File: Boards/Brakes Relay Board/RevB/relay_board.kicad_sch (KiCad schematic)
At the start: 9 parts, among them J1 Screw_Terminal_01x04, J2 Screw_Terminal_01x04, J3 Screw_Terminal_01x04, J4 Screw_Terminal_01x04, J5 Conn_02x10_Counter_Clockwise, J6 Conn_02x12_Counter_Clockwise, J7 Screw_Terminal_01x04

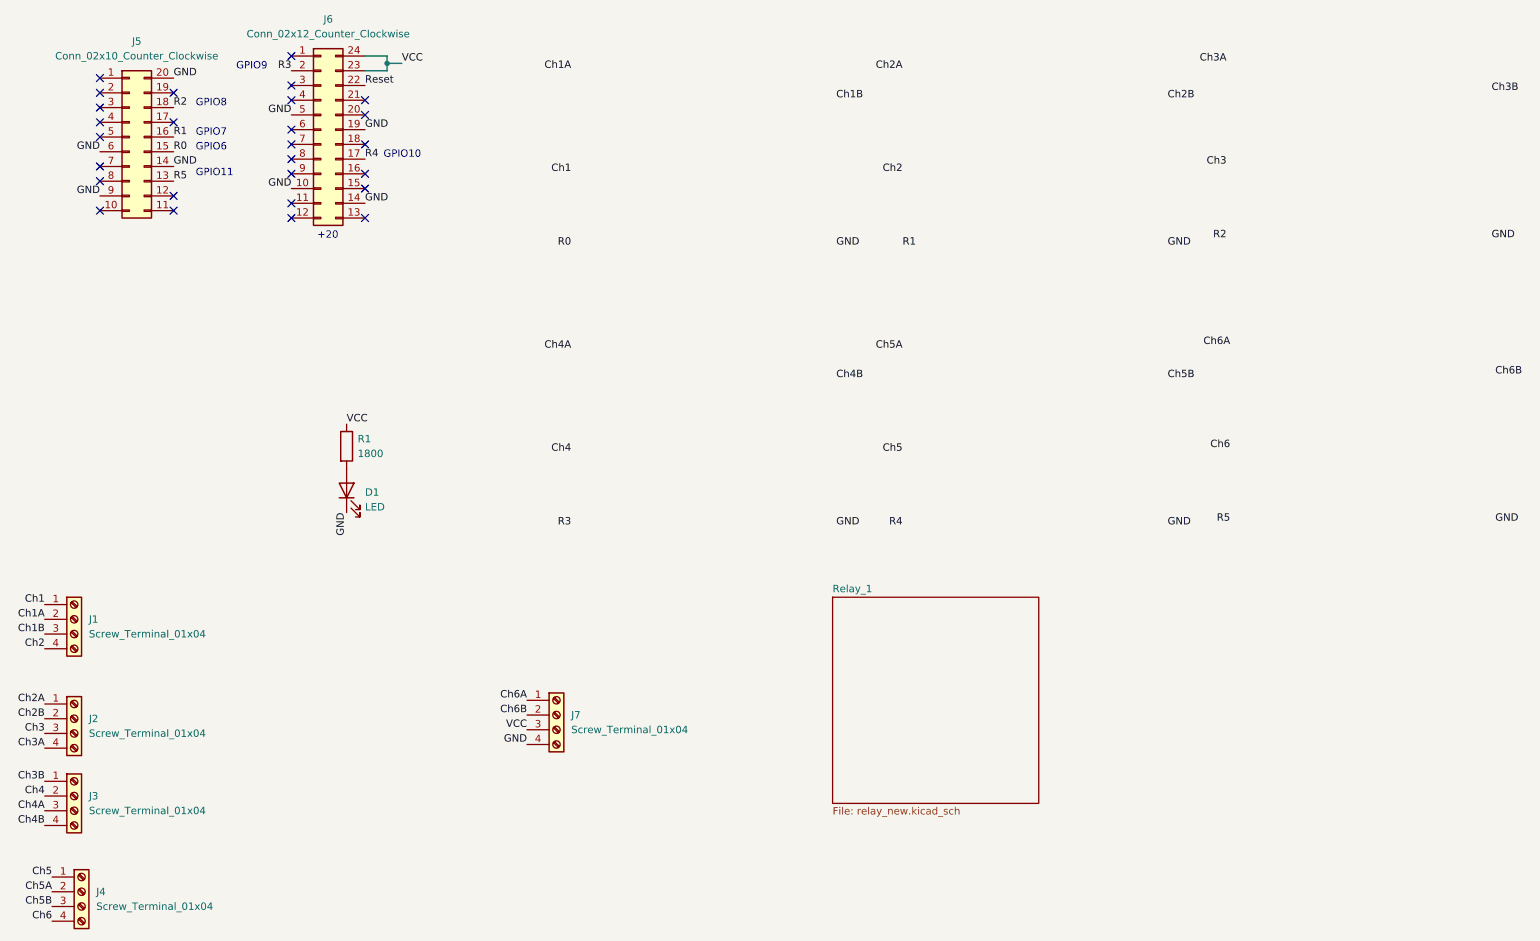
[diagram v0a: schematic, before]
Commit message: Added mosfet to relay and 5V regulator to schematic
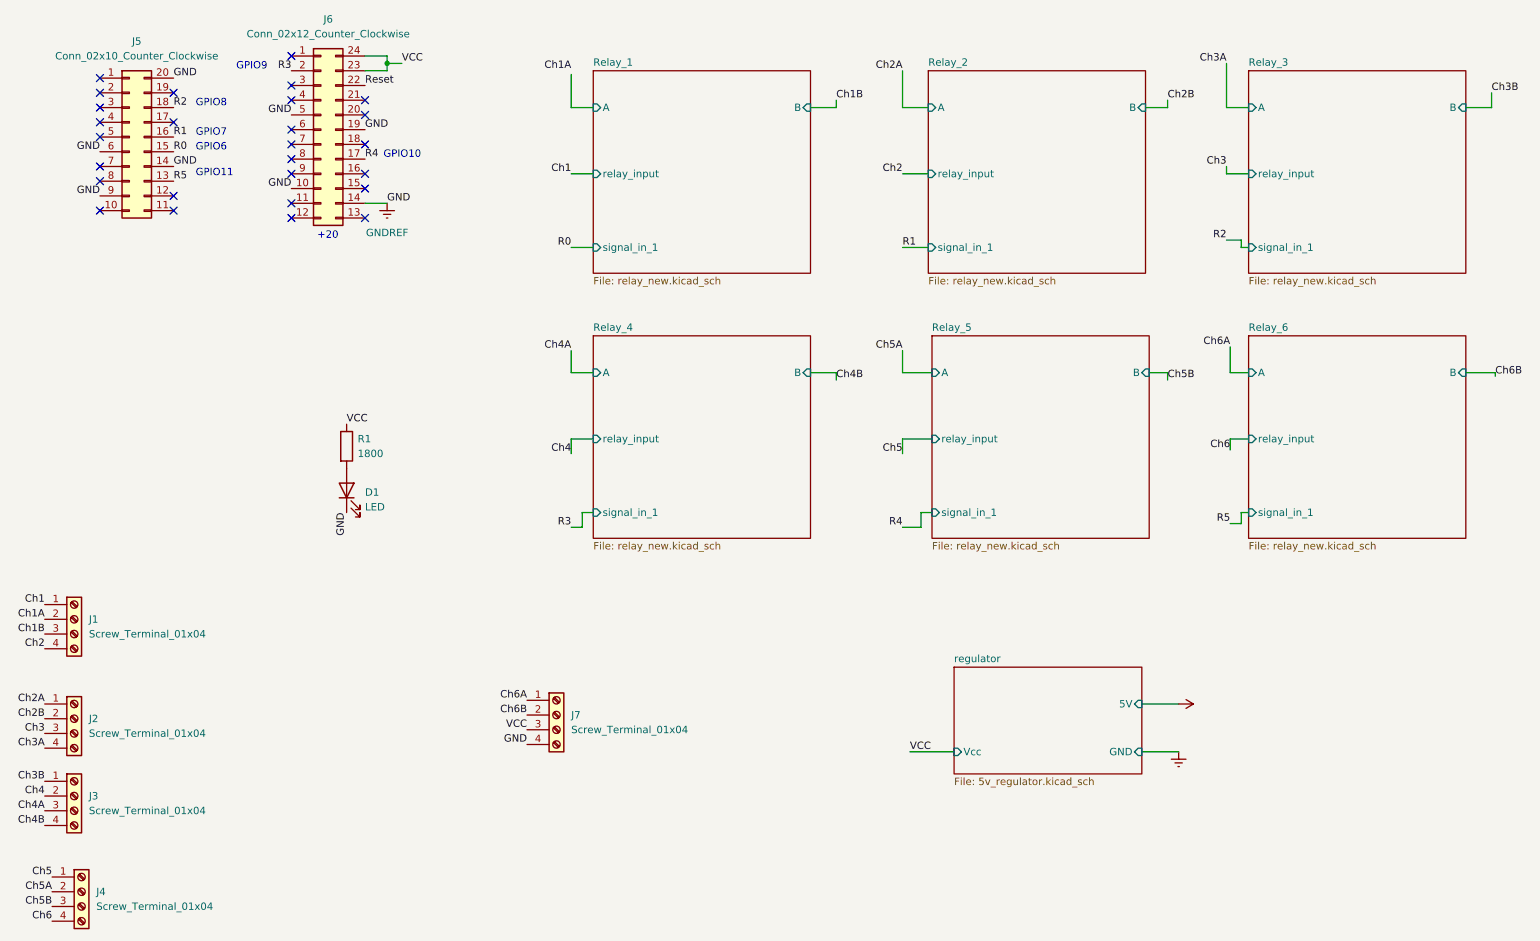
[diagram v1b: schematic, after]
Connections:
- net GND renamed GNDREF
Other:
- added sheet Relay_2 (relay_new.kicad_sch)
- added sheet Relay_3 (relay_new.kicad_sch)
- added sheet Relay_4 (relay_new.kicad_sch)
- added sheet Relay_5 (relay_new.kicad_sch)
- added sheet Relay_6 (relay_new.kicad_sch)
- added sheet regulator (5v_regulator.kicad_sch)
- sheet Relay_1 ports: added A, B, relay_input, signal_in_1; removed none

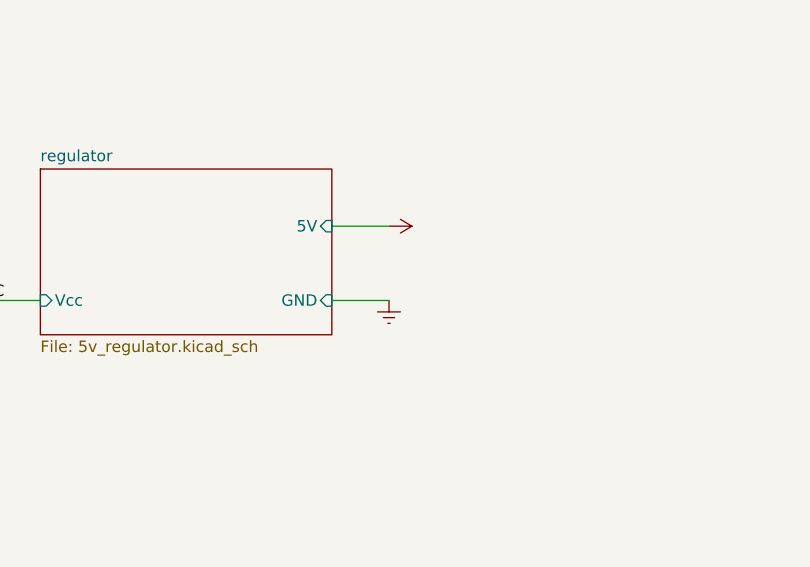
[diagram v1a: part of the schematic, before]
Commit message: Added new components to PCB
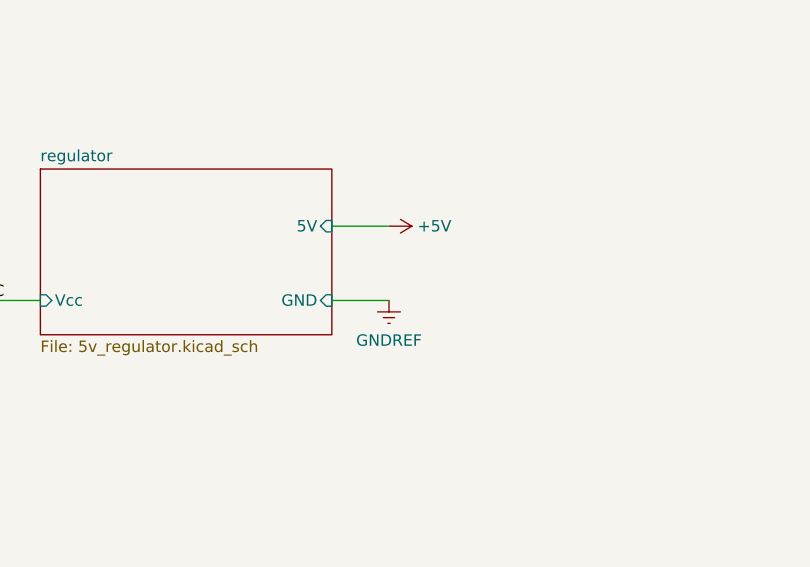
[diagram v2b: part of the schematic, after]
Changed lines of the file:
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@@
       (effects (font (size 1.27 1.27)) hide)
     )
-    (property "Value" "" (id 1) (at 227.33 134.6199 90)
+    (property "Value" "+5V" (id 1) (at 227.33 134.6199 90)
       (effects (font (size 1.27 1.27)) (justify left))
     )
@@
       (effects (font (size 1.27 1.27)) hide)
     )
-    (property "Value" "" (id 1) (at 224.155 147.32 0))
+    (property "Value" "GNDREF" (id 1) (at 224.155 147.32 0))
     (property "Footprint" "" (id 2) (at 224.155 142.875 0)
       (effects (font (size 1.27 1.27)) hide)
@@
     )
     (path "/bd572dac-350f-4d4c-bd5b-e852715803a2/881245eb-3a44-4ffb-9d98-3f402eae8917"
-      (reference "MOSFET1") (unit 1) (value "AOD4184A") (footprint "TO252_AOS")
+      (reference "MOSFET1") (unit 1) (value "AOD4184A") (footprint "BAJA_AOD:AOD4184A")
     )
     (path "/68d18a55-0f25-4a8b-a0f5-d3973226f9cb/881245eb-3a44-4ffb-9d98-3f402eae8917"
-      (reference "MOSFET2") (unit 1) (value "AOD4184A") (footprint "TO252_AOS")
+      (reference "MOSFET2") (unit 1) (value "AOD4184A") (footprint "BAJA_AOD:AOD4184A")
     )
     (path "/f671829b-f8e9-478b-b1dd-c1bafb5bfd9e/881245eb-3a44-4ffb-9d98-3f402eae8917"
-      (reference "MOSFET3") (unit 1) (value "AOD4184A") (footprint "TO252_AOS")
+      (reference "MOSFET3") (unit 1) (value "AOD4184A") (footprint "BAJA_AOD:AOD4184A")
     )
     (path "/1f2ceaa7-2352-45a1-b251-6cdc3d9f6ef6/881245eb-3a44-4ffb-9d98-3f402eae8917"
-      (reference "MOSFET4") (unit 1) (value "AOD4184A") (footprint "TO252_AOS")
+      (reference "MOSFET4") (unit 1) (value "AOD4184A") (footprint "BAJA_AOD:AOD4184A")
     )
     (path "/8fdf32b2-228b-487b-8402-b68dda55aaa8/881245eb-3a44-4ffb-9d98-3f402eae8917"
-      (reference "MOSFET5") (unit 1) (value "AOD4184A") (footprint "TO252_AOS")
+      (reference "MOSFET5") (unit 1) (value "AOD4184A") (footprint "BAJA_AOD:AOD4184A")
     )
     (path "/d71c8dd0-e39c-4a3b-a8be-08e4c9a759a1/881245eb-3a44-4ffb-9d98-3f402eae8917"
-      (reference "MOSFET6") (unit 1) (value "AOD4184A") (footprint "TO252_AOS")
+      (reference "MOSFET6") (unit 1) (value "AOD4184A") (footprint "BAJA_AOD:AOD4184A")
     )
     (path "/2e7a0426-12c9-4aa5-92b6-63a77b09669e"
@@
     )
     (path "/bd572dac-350f-4d4c-bd5b-e852715803a2/8722c8a4-fdb0-4357-8559-49ae618ba880"
-      (reference "U1") (unit 1) (value "ALQ105") (footprint "PAN_ALQ1_PAN")
+      (reference "U1") (unit 1) (value "ALQ105") (footprint "ALQ105-BAJA-FP:ALQ105")
     )
     (path "/68d18a55-0f25-4a8b-a0f5-d3973226f9cb/8722c8a4-fdb0-4357-8559-49ae618ba880"
-      (reference "U2") (unit 1) (value "ALQ105") (footprint "PAN_ALQ1_PAN")
+      (reference "U2") (unit 1) (value "ALQ105") (footprint "ALQ105-BAJA-FP:ALQ105")
     )
     (path "/f671829b-f8e9-478b-b1dd-c1bafb5bfd9e/8722c8a4-fdb0-4357-8559-49ae618ba880"
-      (reference "U3") (unit 1) (value "ALQ105") (footprint "PAN_ALQ1_PAN")
+      (reference "U3") (unit 1) (value "ALQ105") (footprint "ALQ105-BAJA-FP:ALQ105")
     )
     (path "/1f2ceaa7-2352-45a1-b251-6cdc3d9f6ef6/8722c8a4-fdb0-4357-8559-49ae618ba880"
-      (reference "U4") (unit 1) (value "ALQ105") (footprint "PAN_ALQ1_PAN")
+      (reference "U4") (unit 1) (value "ALQ105") (footprint "ALQ105-BAJA-FP:ALQ105")
     )
     (path "/8fdf32b2-228b-487b-8402-b68dda55aaa8/8722c8a4-fdb0-4357-8559-49ae618ba880"
-      (reference "U5") (unit 1) (value "ALQ105") (footprint "PAN_ALQ1_PAN")
+      (reference "U5") (unit 1) (value "ALQ105") (footprint "ALQ105-BAJA-FP:ALQ105")
     )
     (path "/d71c8dd0-e39c-4a3b-a8be-08e4c9a759a1/8722c8a4-fdb0-4357-8559-49ae618ba880"
-      (reference "U6") (unit 1) (value "ALQ105") (footprint "PAN_ALQ1_PAN")
+      (reference "U6") (unit 1) (value "ALQ105") (footprint "ALQ105-BAJA-FP:ALQ105")
     )
     (path "/895d5ca3-0e9a-421e-88ea-3017edd2db62/00000000-0000-0000-0000-00006168283c"
-      (reference "VR1") (unit 1) (value "~") (footprint "SOT230P700X180-4N")
-    )
-  )
+      (reference "VR1") (unit 1) (value "~") (footprint "LM1117IMPX-5:SOT230P700X180-4N")
+    )
+  )
